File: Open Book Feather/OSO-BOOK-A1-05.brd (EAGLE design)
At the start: 77.5 x 112.3 mm, 130 parts, among them J1 SJ-43514-SMT, J2 10118193-0001LF, Q1 DMG341, Q2 IRLML0100, SW1 SPDT_SWITCH, U1 AP2112-3.3, U2 MCP73831T-2ACI/OT, U3 ATSAMD51J64-TQFP(10X10), U4 GD25Q16C (or GD25Q32C), U5 74AC165D, U6 GD25Q16C (or GD25Q32C), U7 MAX4468EKAT, X1 JSTPH, X2 2x5 0.05" SWD

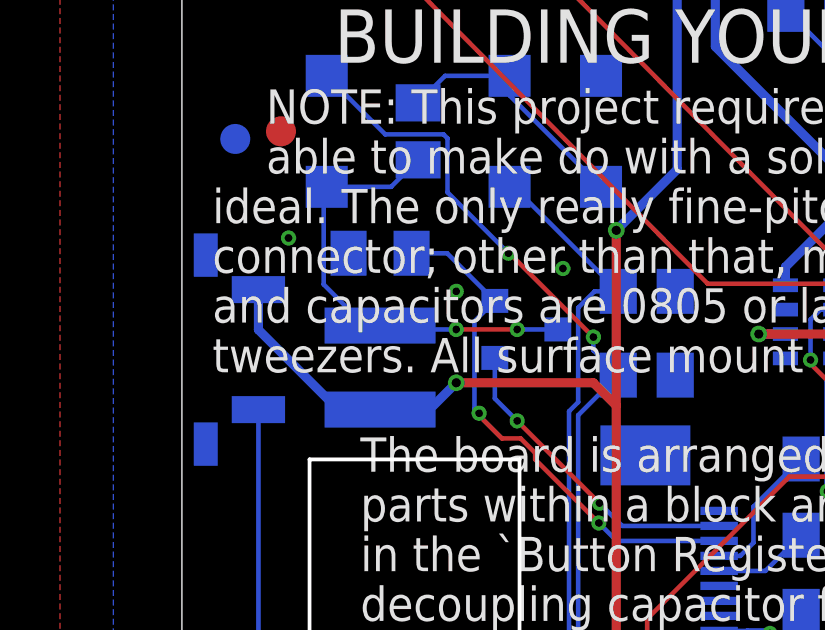
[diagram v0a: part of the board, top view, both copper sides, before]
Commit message: extend inductor's pad out from underneath
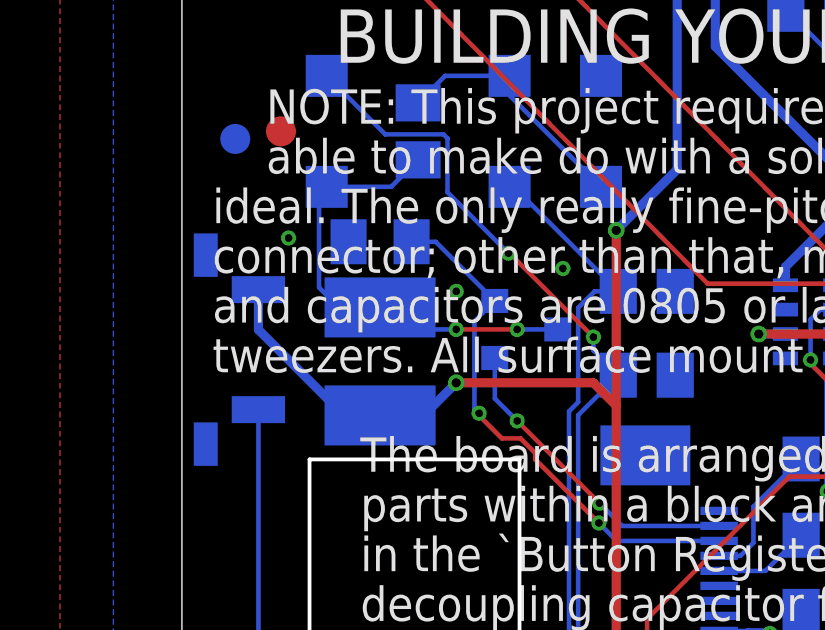
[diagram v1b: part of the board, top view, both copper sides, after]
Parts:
- L1: device microbuilder:INDUCTOR_4X4MM_NR401 -> Adafruit 3.5in 480x320 FeatherWing:MICROBUILDER_INDUCTOR_4X4MM_NR401_BIGPADS
- moved R12 0.38 mm to (6.35, 98.9)
- moved L1 0.20 mm to (6.35, 94.9), turned to 90 degrees
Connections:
- net +3V3: now also L1.P$1; no longer L1.P$2
- net N$3: now also L1.P$2; no longer L1.P$1
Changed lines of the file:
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@@
 <attribute name="VALUE" x="3.302" y="102.616" size="0.508" layer="28" font="vector" ratio="18" rot="MR90" align="center"/>
 </element>
-<element name="L1" library="microbuilder" package="INDUCTOR_4X4MM_NR401" value="10uH" x="6.35" y="94.742" smashed="yes" rot="MR270">
-<attribute name="NAME" x="6.382" y="97.114" size="0.508" layer="26" font="vector" ratio="18" rot="MR180" align="center"/>
-<attribute name="VALUE" x="5.366" y="94.844" size="0.508" layer="28" font="vector" ratio="18" rot="MR180" align="center"/>
-</element>
-<element name="R12" library="microbuilder" package="0805_10MGAP" value="0.47ohm" x="6.35" y="98.552" smashed="yes" rot="MR0">
-<attribute name="NAME" x="6.35" y="99.695" size="0.508" layer="26" font="vector" ratio="18" rot="MR180" align="center"/>
-<attribute name="VALUE" x="9.652" y="98.806" size="0.508" layer="28" font="vector" ratio="18" rot="MR0" align="center"/>
+<element name="R12" library="microbuilder" package="0805_10MGAP" value="0.47ohm" x="6.35" y="98.933" smashed="yes" rot="MR0">
+<attribute name="NAME" x="6.35" y="100.076" size="0.508" layer="26" font="vector" ratio="18" rot="MR180" align="center"/>
+<attribute name="VALUE" x="9.652" y="99.187" size="0.508" layer="28" font="vector" ratio="18" rot="MR0" align="center"/>
 </element>
 <element name="Q2" library="Parts" package="SOT23-3" value="IRLML0100" x="11.176" y="96.012" smashed="yes" rot="MR90">
@@
 <attribute name="NAME" x="24.257" y="2.794" size="0.508" layer="26" font="vector" ratio="18" rot="MR0" align="center"/>
 <attribute name="VALUE" x="22.225" y="0.889" size="0.4064" layer="28" ratio="10" rot="MR0"/>
+</element>
+<element name="L1" library="Adafruit 3.5in 480x320 FeatherWing" package="MICROBUILDER_INDUCTOR_4X4MM_NR401_BIGPADS" value="10uH" x="6.35" y="94.9452" smashed="yes" rot="MR90">
+<attribute name="NAME" x="8.55" y="92.9452" size="0.8128" layer="26" ratio="12" rot="MR90"/>
+<attribute name="VALUE" x="9.55" y="92.9452" size="0.8128" layer="28" ratio="12" rot="MR90"/>
 </element>
 </elements>
@@
 </signal>
 <signal name="+3V3" class="1">
-<contactref element="L1" pad="P$2"/>
 <contactref element="U$2" pad="15"/>
 <contactref element="C17" pad="2"/>
@@
 <wire x1="8.89" y1="94.234" x2="13.462" y2="94.234" width="0.3048" layer="1"/>
 <via x="8.89" y="94.234" extent="1-16" drill="0.3048"/>
-<wire x1="8.89" y1="94.234" x2="7.998" y2="93.342" width="0.3048" layer="16"/>
-<wire x1="7.998" y1="93.342" x2="6.35" y2="93.342" width="0.3048" layer="16"/>
 <via x="42.0624" y="53.2384" extent="1-16" drill="0.3048"/>
 <wire x1="53.721" y1="64.643" x2="42.3164" y2="53.2384" width="0.3048" layer="1"/>
@@
 <wire x1="74.676" y1="78.882" x2="71.374" y2="75.58" width="0.3048" layer="1"/>
 <via x="71.374" y="75.58" extent="1-16" drill="0.3048"/>
-<wire x1="6.35" y1="93.342" x2="4.956" y2="93.342" width="0.3048" layer="16"/>
-<wire x1="2.2956" y1="96.0024" x2="2.2956" y2="97.34" width="0.3048" layer="16"/>
-<wire x1="4.956" y1="93.342" x2="2.2956" y2="96.0024" width="0.3048" layer="16"/>
+<wire x1="2.2956" y1="97.34" x2="2.2956" y2="96.0024" width="0.3048" layer="16"/>
 <contactref element="R13" pad="5"/>
 <wire x1="19.7358" y1="21.1328" x2="18.40805" y2="21.1328" width="0.3048" layer="16"/>
@@
 <wire x1="28.771" y1="1.143" x2="28.4662" y2="0.8382" width="0.3048" layer="16"/>
 <wire x1="28.4662" y1="0.8382" x2="26.0198" y2="0.8382" width="0.3048" layer="16"/>
+<contactref element="L1" pad="P$1"/>
+<wire x1="2.2956" y1="96.0024" x2="5.1528" y2="93.1452" width="0.3048" layer="16"/>
+<wire x1="5.1528" y1="93.1452" x2="6.35" y2="93.1452" width="0.3048" layer="16"/>
+<wire x1="6.35" y1="93.1452" x2="7.8012" y2="93.1452" width="0.3048" layer="16"/>
+<wire x1="7.8012" y1="93.1452" x2="8.89" y2="94.234" width="0.3048" layer="16"/>
 </signal>
 <signal name="GDR">
@@
 <wire x1="11.03788125" y1="92.3785" x2="10.414" y2="92.3785" width="0.1524" layer="1"/>
 <wire x1="17.6532" y1="88.9634" x2="14.2401" y2="88.9634" width="0.1524" layer="16"/>
-<wire x1="10.176" y1="96.962" x2="8.586" y2="98.552" width="0.1524" layer="16"/>
-<wire x1="8.586" y1="98.552" x2="7.4" y2="98.552" width="0.1524" layer="16"/>
+<wire x1="10.176" y1="96.962" x2="8.205" y2="98.933" width="0.1524" layer="16"/>
+<wire x1="8.205" y1="98.933" x2="7.4" y2="98.933" width="0.1524" layer="16"/>
 <wire x1="10.414" y1="92.3785" x2="9.652" y2="93.1405" width="0.1524" layer="1"/>
 <wire x1="9.652" y1="93.1405" x2="9.652" y2="93.218" width="0.1524" layer="1"/>
@@
 <signal name="N$3">
 <contactref element="D4" pad="A"/>
-<contactref element="L1" pad="P$1"/>
 <contactref element="Q2" pad="3"/>
 <contactref element="C24" pad="1"/>
 <wire x1="7.62" y1="101.666" x2="6.72" y2="100.766" width="0.1524" layer="16"/>
 <wire x1="6.72" y1="100.766" x2="4.572" y2="100.766" width="0.1524" layer="16"/>
-<wire x1="4.572" y1="100.766" x2="4.4714" y2="100.6654" width="0.1524" layer="16"/>
-<wire x1="4.4714" y1="100.6654" x2="4.4714" y2="97.5126" width="0.1524" layer="16"/>
-<wire x1="5.842" y1="96.142" x2="4.4714" y2="97.5126" width="0.1524" layer="16"/>
-<wire x1="5.842" y1="96.142" x2="6.35" y2="96.142" width="0.1524" layer="16"/>
-<wire x1="6.35" y1="96.012" x2="6.35" y2="96.142" width="0.1524" layer="16"/>
 <wire x1="12.276" y1="96.012" x2="10.922" y2="96.012" width="0.1524" layer="16"/>
 <via x="10.922" y="96.012" extent="1-16" drill="0.254"/>
 <wire x1="10.922" y1="96.012" x2="8.89" y2="96.012" width="0.1524" layer="1"/>
 <via x="8.89" y="96.012" extent="1-16" drill="0.254"/>
-<wire x1="8.89" y1="96.012" x2="6.35" y2="96.012" width="0.1524" layer="16"/>
+<contactref element="L1" pad="P$2"/>
+<wire x1="4.572" y1="100.766" x2="4.318" y2="100.512" width="0.1524" layer="16"/>
+<wire x1="4.318" y1="100.512" x2="4.318" y2="97.409" width="0.1524" layer="16"/>
+<wire x1="4.318" y1="97.409" x2="4.9818" y2="96.7452" width="0.1524" layer="16"/>
+<wire x1="4.9818" y1="96.7452" x2="6.35" y2="96.7452" width="0.1524" layer="16"/>
+<wire x1="6.35" y1="96.7452" x2="7.0832" y2="96.012" width="0.1524" layer="16"/>
+<wire x1="7.0832" y1="96.012" x2="8.89" y2="96.012" width="0.1524" layer="16"/>
 </signal>
 <signal name="A9_">

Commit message: DNP side buttons
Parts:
- renumbered BTN_NEXT_ALT to DNP_NEXT_ALT, BTN_PREV_ALT to DNP_PREV_ALT
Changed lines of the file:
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@@
 <setting verticaltext="up"/>
 </settings>
-<grid distance="0.005" unitdist="inch" unit="inch" style="lines" multiple="1" display="no" altdistance="0.001" altunitdist="inch" altunit="inch"/>
+<grid distance="0.01" unitdist="inch" unit="inch" style="lines" multiple="1" display="no" altdistance="0.001" altunitdist="inch" altunit="inch"/>
 <layers>
 <layer number="1" name="Top" color="4" fill="1" visible="yes" active="yes"/>
@@
 <attribute name="NAME" x="8.636" y="7.493" size="0.8128" layer="52" font="vector" ratio="18" rot="MR0" align="center"/>
 </element>
-<element name="BTN_PREV_ALT" library="My Stuff" package="TL3330AF130QG" value="SPST_TACTILE_SWITCHRA" x="2.6416" y="91.44" smashed="yes" rot="MR90"/>
+<element name="DNP_PREV_ALT" library="My Stuff" package="TL3330AF130QG" value="SPST_TACTILE_SWITCHRA" x="2.6416" y="91.44" smashed="yes" rot="MR90"/>
 <element name="PORT_A9" library="microbuilder" package="JSTPH3" value="JST PH 3" x="4.318" y="70.104" smashed="yes" rot="MR270">
 <attribute name="NAME" x="10.668" y="70.1515" size="0.8128" layer="26" font="vector" ratio="18" rot="MR270" align="center"/>
@@
 <attribute name="VALUE" x="27.94" y="26.4922" size="0.508" layer="28" font="vector" ratio="18" rot="MR180" align="center"/>
 </element>
-<element name="BTN_NEXT_ALT" library="My Stuff" package="TL3330AF130QG" value="SPST_TACTILE_SWITCHRA" x="74.3204" y="90.8558" smashed="yes" rot="MR270"/>
+<element name="DNP_NEXT_ALT" library="My Stuff" package="TL3330AF130QG" value="SPST_TACTILE_SWITCHRA" x="74.3204" y="90.8558" smashed="yes" rot="MR270"/>
 <element name="JP1" library="adafruit" package="1X03" value="" x="8.636" y="108.839" smashed="yes" rot="MR0">
 <attribute name="VALUE" x="12.446" y="105.664" size="1.27" layer="28" rot="MR0"/>
@@
 <wire x1="23.241" y1="16.2306" x2="20.828" y2="13.8176" width="0.3048" layer="16"/>
 <wire x1="20.828" y1="13.8176" x2="18.40805" y2="16.23755" width="0.3048" layer="16"/>
-<contactref element="BTN_PREV_ALT" pad="P$2"/>
-<contactref element="BTN_NEXT_ALT" pad="P$2"/>
+<contactref element="DNP_PREV_ALT" pad="P$2"/>
+<contactref element="DNP_NEXT_ALT" pad="P$2"/>
 <wire x1="74.6664" y1="84.9558" x2="74.676" y2="84.9462" width="0.3048" layer="16"/>
 <wire x1="74.676" y1="84.9462" x2="74.676" y2="82.804" width="0.3048" layer="16"/>
@@
 <wire x1="22.3774" y1="23.61434375" x2="22.68985625" y2="23.9268" width="0.1524" layer="16"/>
 <wire x1="22.20613125" y1="22.7584" x2="22.3774" y2="22.92966875" width="0.1524" layer="16"/>
-<contactref element="BTN_PREV_ALT" pad="P$1"/>
+<contactref element="DNP_PREV_ALT" pad="P$1"/>
 <wire x1="2.2956" y1="93.34" x2="2.2956" y2="76.9716" width="0.1524" layer="16"/>
 <wire x1="2.2956" y1="76.9716" x2="1.524" y2="76.2" width="0.1524" layer="16"/>
@@
 <signal name="BUTTON6">
 <contactref element="U5" pad="5"/>
-<contactref element="BTN_NEXT_ALT" pad="P$1"/>
+<contactref element="DNP_NEXT_ALT" pad="P$1"/>
 <wire x1="74.6664" y1="88.9558" x2="74.6664" y2="86.6180875" width="0.1524" layer="16"/>
 <wire x1="74.6664" y1="86.6180875" x2="73.5488" y2="85.5004875" width="0.1524" layer="16"/>

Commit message: last tweaks to A1-05 before sending to fab
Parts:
- removed U$44: OSO_GRAPHIC, My Stuff:OSO_GRAPHIC
- added U$49: (no value), My Stuff:OSO_WORDMARK_THREELINE_450MIL_1000DPI
- U$45: value OSO_BEAR -> (none); device My Stuff:OSO_BEAR_750MIL -> My Stuff:OSO_WORDMARK_125X1300MIL_1000DPI
- U$47: value OSO_TEXT -> (none); device My Stuff:OSO_TEXT_435MIL -> My Stuff:OSO_BEAR_525X750MIL_1000DPI
- U$48: value OSO_TEXTOSO_TEXT_ONELINE_125MIL -> (none); device My Stuff:OSO_ONELINE_125MIL -> Oddly Specific Artwork:OSO-LOGO-250MIL
- moved U$45 79.9 mm to (43.7, 14.5), flipped to the top
- moved U$48 40.5 mm to (3.81, 12.4), turned to 45 degrees
- moved U$47 15.9 mm to (38.6, 94.7)
- moved C13 1.02 mm to (15.5, 7.37)
- moved D4 1.02 mm to (3.56, 102.6)
- moved R8 1.02 mm to (21.1, 7.37)
- moved R9 1.02 mm to (18.3, 7.37)
- moved SW1 0.99 mm to (9.27, 3.81)
- moved C24 0.76 mm to (6.86, 102.6)
- moved D3 0.51 mm to (10.2, 102.6)
- moved R4 0.25 mm to (24.9, 107.0)
- moved D2 0.25 mm to (13.5, 102.6)
- moved R12 0.25 mm to (6.35, 99.2)
- moved R5 0.25 mm to (20.8, 106.9)
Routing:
- net SWO: track 85.8 -> 83.0 mm, vias 2 -> 4
- net N$70: track 8.23 -> 5.41 mm
- net N$15: track 8.26 -> 5.53 mm
- net !RESET: track 156.9 -> 155.8 mm
- net EN: track 150.0 -> 151.0 mm
- net +3V3: track 513.3 -> 512.4 mm
- net PREVGH: track 33.3 -> 34.1 mm
- net N$1: track 4.03 -> 4.90 mm
- net PREVGL: track 27.4 -> 27.9 mm
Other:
- board text added: "(R21-C33)"
- board text added: "...on A10/PA07. Turn the amplifier off by setting D48/PB31 high. This also powers down the mic bias circuit to save some power."
- board text added: "BTN_NEXT_ALT"
- board text added: "BTN_PREV_ALT"
- board text added: "BUTTON_CLOCK=D53=PB14 BUTTON_OUT=D49=PB30 BUTTON_LATCH=D43=PB12"
- board text added: "Bits: 0: Left 1: Down 2: Up 3: Rt 4: Sel 5: Prev 6: Next 7: SD"
- board text added: "D1, Q1&R2 conspire to let only the higher of VBAT and VBUS reach 3.3V regulator U1. C1 filters regulator input; C2 & C3 filter output. R1 pulls EN high to keep the regulator on. BATTERY: U2 is a LiPo charging controller. Powered by VBUS, it charges the battery at a rate determined by R3. C4=filter for VBAT, R4&R5 limit current to CHG & FUL LEDs. R6: voltage dividers to gauge VBAT and VBUS on A6/P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"
- board text added: "Lots to unpack here. For starters, the Feather pinout is mostly identical to the Adafruit SAMD51 boards you're familiar with, PWM & analog pins where you expect them (minus ``extra'' pin D4). SERCOM5: Serial (RX/TX = D0/D1 = PB17/PB16) SERCOM1: SPI (MOSI/MISO/SCK = D27/D26/D28 = PB23/PB22/PA17) SERCOM2: I²C (SDA/SCL = D24/D25 = PA12/PA13) SERCOM4: SPI for the display: MOSI1/SCK1 = D41/D42 = PB15/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"
- board text added: "OSO-BOOK-A1-05"
- board text added: "R1 up top pulls EN high. Switching SW1 pulls EN low, disabling pwr supply U1 (along with most of the board.)"
- board text added: "R8: pull-up for !RESET!. Btn pulls it low; C13&R9 help. Double tap for UF2 bootloader."
- board text added: "These resistors and capacitors couple analog outputs A0/PA02 and A1/PA05 to R and L channels of the audio jack. A7/PB04 is raw signal from mic input."
- board text removed: "...on A10/PA07. Turn the amplifier off by setting D48/PB31 high. This also powers down the mic bias circuit R21-C33 to save some power."
- board text removed: "BTN_NEXT"
- board text removed: "BTN_PREV"
- board text removed: "Bits: 0: Left 1: Down 2: Up 3: Right 4: Select 5: Previous 6: Next 7: SD"
- board text removed: "D1&Q1 conspire to let only the higher of VBAT & VBUS reach 3.3V regulator U1. C1 filters regulator input; C2 & C3 filter output. R1 pulls EN high to keep the regulator on. BATTERY: U2 is a LiPo charging controller. Powered by VBUS, it charges the battery at a rate determined by R3. C4=filter for VBAT, R4&R5 limit current to CHG & FUL LEDs. R6: voltage dividers to gauge VBAT and VBUS on A6/PB01 an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"
- board text removed: "Lots to unpack here. For starters, the Feather pinout is mostly identical to the Adafruit SAMD51 boards you're familiar with, PWM & analog pins where you expect them (minus "extra" pin D4). SERCOM5: Serial (RX/TX = D0/D1 = PB17/PB16) SERCOM1: SPI (MOSI/MISO/SCK = D27/D26/D28 = PB23/PB22/PA17) SERCOM2: I²C (SDA/SCL = D24/D25 = PA12/PA13) SERCOM4: SPI for the display: MOSI1/SCK1 = D41/D42 = PB15/PB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"
- board text removed: "OSO-BOOK-A1-06"
- board text removed: "Pins: BUTTON_CLOCK: D53/PB14 BUTTON_OUT: D49/PB30 BUTTON_LATCH: D43/PB12"
- board text removed: "R1 up top pulls EN high. Switching SW1 pulls EN low, disabling pwr supply U1 along with most of the board."
- board text removed: "R8 pulls !RESET high. Btn pulls it low; C13 & R9 help. Double tap for UF2 bootloader."
- board text removed: "These resistors and capacitors couple analog outputs A0/PA02 and A1/PA05 to R and L channels of the phone jack. A7/PB04 is raw signal from mic input."

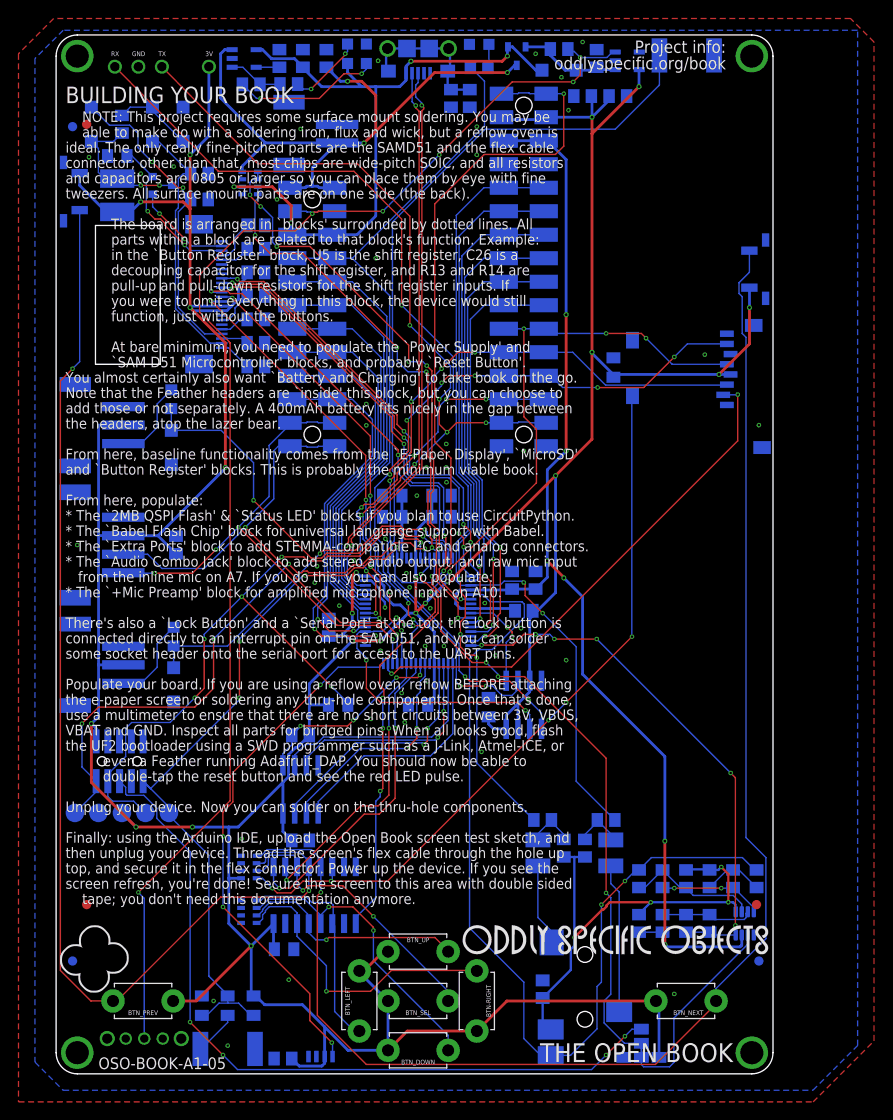
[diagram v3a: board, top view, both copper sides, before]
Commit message: Buttons & SD card change
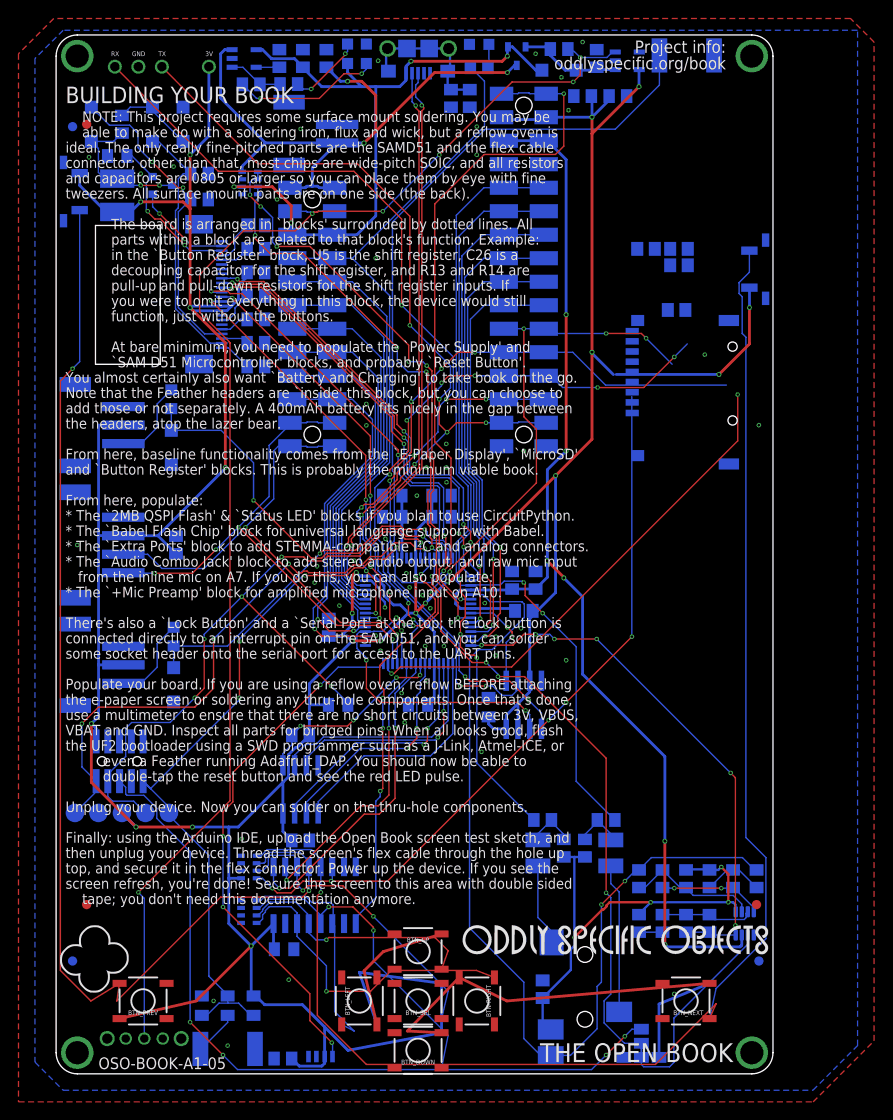
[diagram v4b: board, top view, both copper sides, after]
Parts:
- removed C25: 10uF, microbuilder:0805_10MGAP
- removed MICROSD: MICROSD, adafruit:MICROSD
- added C37: 10uF, rcl:C0805
- added R28, R29, R30: 10K, rcl:R0805
- added SD_CARD: MICRO_SD_CARD_, dronecz:TFP09-2--12B
- BTN-RIGHT, BTN_DOWN, BTN_LEFT, BTN_NEXT, BTN_PREV, BTN_SEL, BTN_UP: value (none) -> TACTILE_SWITCHE_5X5_MICRO_; device adafruit:TACT_PANA-EVQ -> dronecz:TACTILE_SWITCH_5X5_MICRO
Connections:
- net +3V3: now also BTN-RIGHT.3, BTN_DOWN.3, BTN_LEFT.3, BTN_NEXT.3, BTN_PREV.3, BTN_SEL.3, BTN_UP.3, C37.1, R28.2, R29.2, R30.2, SD_CARD.VCC; no longer BTN-RIGHT.P$2, BTN_DOWN.P$2, BTN_LEFT.P$2, BTN_NEXT.P$2, BTN_PREV.P$2, BTN_SEL.P$2, BTN_UP.P$2, C25.1, MICROSD.4
- net BUTTON0: now also BTN_LEFT.1; no longer BTN_LEFT.P$1
- net BUTTON1: now also BTN_DOWN.1; no longer BTN_DOWN.P$1
- net BUTTON2: now also BTN_UP.1; no longer BTN_UP.P$1
- net BUTTON3: now also BTN-RIGHT.1; no longer BTN-RIGHT.P$1
- net BUTTON4: now also BTN_SEL.1; no longer BTN_SEL.P$1
- net BUTTON5: now also BTN_PREV.1; no longer BTN_PREV.P$1
- net BUTTON6: now also BTN_NEXT.1, BTN_NEXT.2; no longer BTN_NEXT.P$1
- net BUTTON7: now also SD_CARD.CD; no longer MICROSD.CD2
- net GND: now also C37.2, SD_CARD.GND, SD_CARD.GND@1, SD_CARD.GND@2, SD_CARD.GND@3, SD_CARD.VSS; no longer C25.2, MICROSD.6, MICROSD.MT1, MICROSD.MT2
- net MISO: now also R30.1, SD_CARD.DAT0; no longer MICROSD.7
- net MOSI: now also R28.1, SD_CARD.CMD; no longer MICROSD.3
- net SCK: now also R29.1, SD_CARD.CLK; no longer MICROSD.5
- net SDCS: now also SD_CARD.CD/DAT3; no longer MICROSD.2
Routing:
- net +3V3: track 512.4 -> 558.1 mm
- net SCK: track 98.8 -> 92.8 mm
- net MISO: track 81.3 -> 77.0 mm
- net BUTTON6: track 158.0 -> 161.4 mm
- net BUTTON5: track 126.3 -> 129.1 mm
- net BUTTON2: track 25.0 -> 27.0 mm
- net BUTTON3: track 32.7 -> 34.8 mm
- net BUTTON4: track 31.2 -> 33.1 mm
- net BUTTON1: track 32.6 -> 34.5 mm
- net SDCS: track 55.7 -> 54.1 mm
- net BUTTON0: track 24.0 -> 25.0 mm
